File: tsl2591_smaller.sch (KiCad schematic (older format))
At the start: 7 parts, among them J1 Conn_01x04_Female, Q1 BSS138, Q2 BSS138, U1 TSL2591

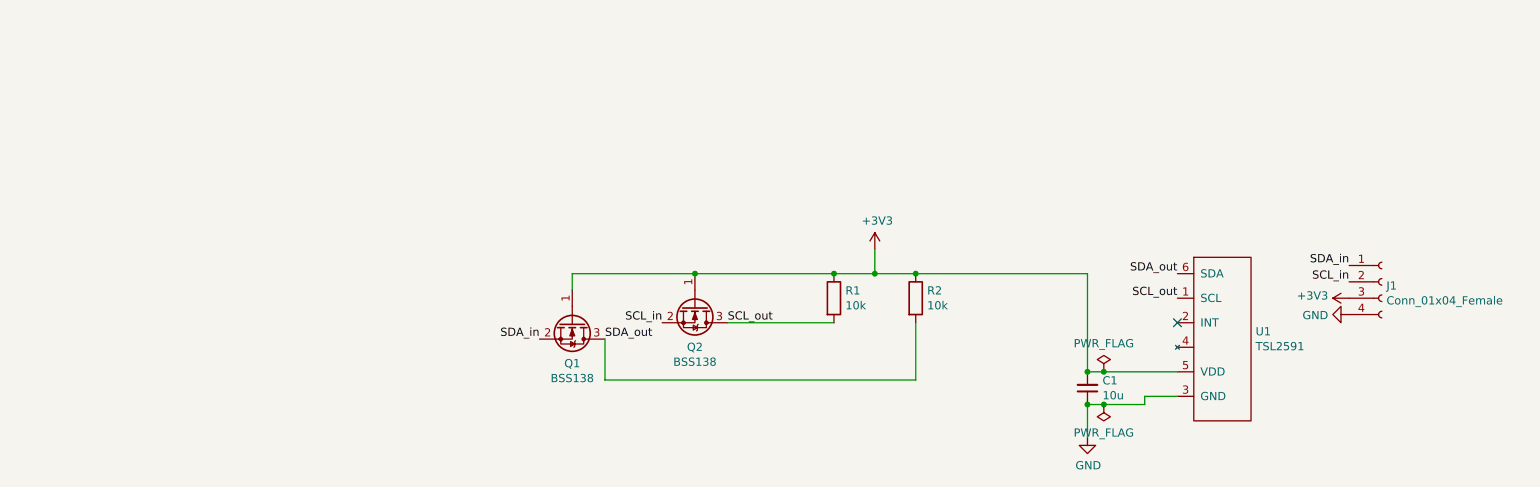
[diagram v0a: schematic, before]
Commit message: Removed more components
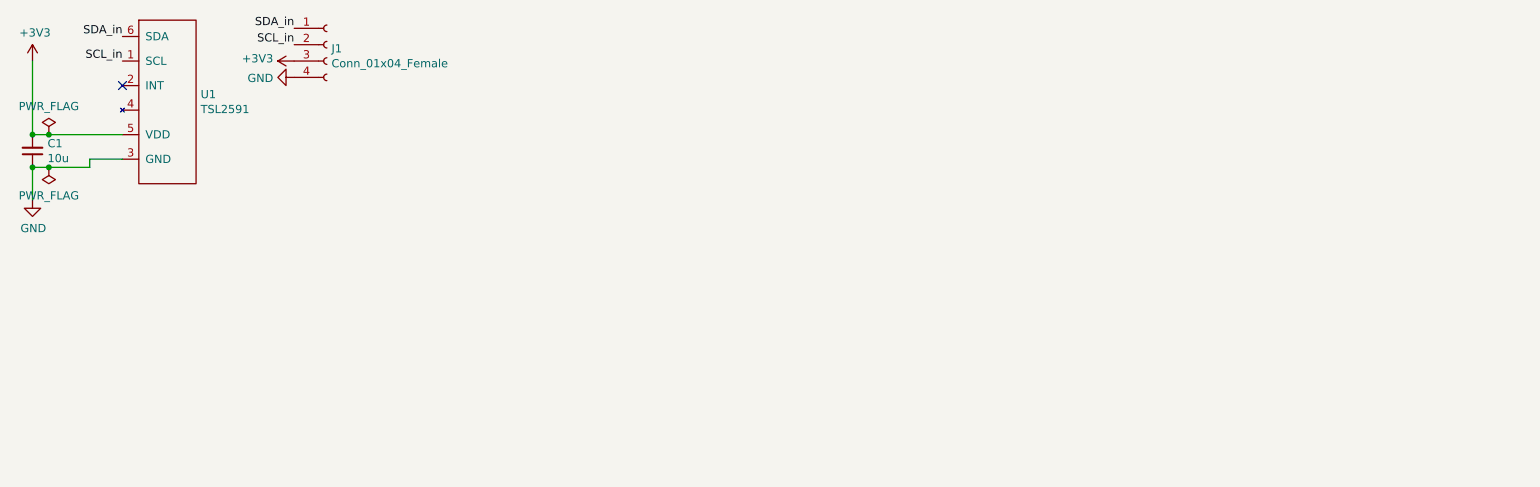
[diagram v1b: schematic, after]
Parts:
- removed Q1, Q2: BSS138, TO_SOT_Packages_SMD:SOT-23, symbol Transistor_FET:BSS138
- removed R1, R2: 10k, Resistors_SMD:R_0805, symbol Device:R
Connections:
- net SCL_out is gone; now on net SCL_in: U1.1 (SCL)
- net SDA_out is gone; now on net SDA_in: U1.6 (SDA)
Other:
- moved on the sheet: C1, J1, U1
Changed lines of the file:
@@
 encoding utf-8
 Sheet 1 1
-Title ""
-Date ""
-Rev ""
-Comp ""
-Comment1 ""
-Comment2 ""
+Title "TSL2591 Board"
+Date "2021-03-06"
+Rev "1.0.0"
+Comp "UTSVT"
+Comment1 "Matthew Yu"
+Comment2 "Jacob Pustilnik"
 Comment3 ""
 Comment4 ""
 $EndDescr
 $Comp
-L Transistor_FET:BSS138 Q1
-U 1 1 6004C224
-P 4350 2650
-F 0 "Q1" V 4599 2650 50  0000 C CNN
-F 1 "BSS138" V 4690 2650 50  0000 C CNN
-F 2 "TO_SOT_Packages_SMD:SOT-23" H 4550 2575 50  0001 L CIN
-F 3 "https://www.fairchildsemi.com/datasheets/BS/BSS138.pdf" H 4350 2650 50  0001 L CNN
-	1    4350 2650
-	0    1    1    0
-$EndComp
-$Comp
-L Transistor_FET:BSS138 Q2
-U 1 1 6004F25D
-P 5100 2550
-F 0 "Q2" V 5349 2550 50  0000 C CNN
-F 1 "BSS138" V 5440 2550 50  0000 C CNN
-F 2 "TO_SOT_Packages_SMD:SOT-23" H 5300 2475 50  0001 L CIN
-F 3 "https://www.fairchildsemi.com/datasheets/BS/BSS138.pdf" H 5100 2550 50  0001 L CNN
-	1    5100 2550
-	0    1    1    0
-$EndComp
-$Comp
-L Device:R R1
-U 1 1 6005217F
-P 5950 2500
-F 0 "R1" H 6020 2546 50  0000 L CNN
-F 1 "10k" H 6020 2455 50  0000 L CNN
-F 2 "Resistors_SMD:R_0805" V 5880 2500 50  0001 C CNN
-F 3 "~" H 5950 2500 50  0001 C CNN
-	1    5950 2500
+L power:+3V3 #PWR01
+U 1 1 60054825
+P 1050 1050
+F 0 "#PWR01" H 1050 900 50  0001 C CNN
+F 1 "+3V3" H 1065 1223 50  0000 C CNN
+F 2 "" H 1050 1050 50  0001 C CNN
+F 3 "" H 1050 1050 50  0001 C CNN
+	1    1050 1050
 	1    0    0    -1
 $EndComp
 $Comp
-L power:+3V3 #PWR01
-U 1 1 60054825
-P 6200 2200
-F 0 "#PWR01" H 6200 2050 50  0001 C CNN
-F 1 "+3V3" H 6215 2373 50  0000 C CNN
-F 2 "" H 6200 2200 50  0001 C CNN
-F 3 "" H 6200 2200 50  0001 C CNN
-	1    6200 2200
-	1    0    0    -1
+L tsl2591_smaller:TSL2591 U1
+U 1 1 60064A60
+P 2200 1300
+F 0 "U1" V 2154 1178 50  0000 L CNN
+F 1 "TSL2591" V 2245 1178 50  0000 L CNN
+F 2 "tsl2591_smaller:tsl2591" H 2200 1300 50  0001 C CNN
+F 3 "" H 2200 1300 50  0001 C CNN
+	1    2200 1300
+	0    1    1    0
 $EndComp
+Wire Wire Line
+	1050 1500 1150 1500
 $Comp
-L Device:R R2
-U 1 1 60053D35
-P 6450 2500
-F 0 "R2" H 6520 2546 50  0000 L CNN
-F 1 "10k" H 6520 2455 50  0000 L CNN
-F 2 "Resistors_SMD:R_0805" V 6380 2500 50  0001 C CNN
-F 3 "~" H 6450 2500 50  0001 C CNN
-	1    6450 2500
+L Device:C_Small C1
+U 1 1 6006B095
+P 1050 1600
+F 0 "C1" H 958 1554 50  0000 R CNN
+F 1 "10u" H 958 1645 50  0000 R CNN
+F 2 "Resistors_SMD:R_0805" H 1050 1600 50  0001 C CNN
+F 3 "~" H 1050 1600 50  0001 C CNN
+	1    1050 1600
+	-1   0    0    1
+$EndComp
+Wire Wire Line
+	1050 1700 1150 1700
+Wire Wire Line
+	1400 1700 1400 1650
+$Comp
+L power:GND #PWR02
+U 1 1 6006E387
+P 1050 1900
+F 0 "#PWR02" H 1050 1650 50  0001 C CNN
+F 1 "GND" H 1055 1727 50  0000 C CNN
+F 2 "" H 1050 1900 50  0001 C CNN
+F 3 "" H 1050 1900 50  0001 C CNN
+	1    1050 1900
 	1    0    0    -1
 $EndComp
 Wire Wire Line
-	5950 2350 6200 2350
-Wire Wire Line
-	6200 2200 6200 2350
-Connection ~ 6200 2350
-Wire Wire Line
-	6200 2350 6450 2350
-Wire Wire Line
-	5950 2350 5100 2350
-Connection ~ 5950 2350
-Wire Wire Line
-	5100 2350 4350 2350
-Wire Wire Line
-	4350 2350 4350 2450
-Connection ~ 5100 2350
-Text Label 4150 2750 2    50   ~ 0
+	1050 1900 1050 1700
+Connection ~ 1050 1700
+Text Label 1600 1050 2    50   ~ 0
+SCL_in
+NoConn ~ 1600 1200
+Text Label 1600 900  2    50   ~ 0
 SDA_in
-Text Label 4550 2750 0    50   ~ 0
-SDA_out
-Text Label 4900 2650 2    50   ~ 0
-SCL_in
-Text Label 5300 2650 0    50   ~ 0
-SCL_out
-Wire Wire Line
-	5950 2650 5300 2650
-Wire Wire Line
-	6450 2650 6450 3000
-Wire Wire Line
-	6450 3000 4550 3000
-Wire Wire Line
-	4550 3000 4550 2750
-$Comp
-L tsl2591_smaller:TSL2591 U1
-U 1 1 60064A60
-P 8650 2750
-F 0 "U1" V 8604 2628 50  0000 L CNN
-F 1 "TSL2591" V 8695 2628 50  0000 L CNN
-F 2 "tsl2591_smaller:tsl2591" H 8650 2750 50  0001 C CNN
-F 3 "" H 8650 2750 50  0001 C CNN
-	1    8650 2750
-	0    1    1    0
-$EndComp
-Wire Wire Line
-	6450 2350 7500 2350
-Wire Wire Line
-	7500 2350 7500 2950
-Wire Wire Line
-	7500 2950 7600 2950
-Connection ~ 6450 2350
-$Comp
-L Device:C_Small C1
-U 1 1 6006B095
-P 7500 3050
-F 0 "C1" H 7408 3004 50  0000 R CNN
-F 1 "10u" H 7408 3095 50  0000 R CNN
-F 2 "Resistors_SMD:R_0805" H 7500 3050 50  0001 C CNN
-F 3 "~" H 7500 3050 50  0001 C CNN
-	1    7500 3050
-	-1   0    0    1
-$EndComp
-Connection ~ 7500 2950
-Wire Wire Line
-	7500 3150 7600 3150
-Wire Wire Line
-	7850 3150 7850 3100
-$Comp
-L power:GND #PWR02
-U 1 1 6006E387
-P 7500 3350
-F 0 "#PWR02" H 7500 3100 50  0001 C CNN
-F 1 "GND" H 7505 3177 50  0000 C CNN
-F 2 "" H 7500 3350 50  0001 C CNN
-F 3 "" H 7500 3350 50  0001 C CNN
-	1    7500 3350
-	1    0    0    -1
-$EndComp
-Wire Wire Line
-	7500 3350 7500 3150
-Connection ~ 7500 3150
-Text Label 8050 2500 2    50   ~ 0
-SCL_out
-NoConn ~ 8050 2650
-Text Label 8050 2350 2    50   ~ 0
-SDA_out
 $Comp
 L power:+3V3 #PWR03
 U 1 1 6007AD26
-P 9100 2500
-F 0 "#PWR03" H 9100 2350 50  0001 C CNN
-F 1 "+3V3" V 9115 2628 50  0000 L CNN
-F 2 "" H 9100 2500 50  0001 C CNN
-F 3 "" H 9100 2500 50  0001 C CNN
-	1    9100 2500
+P 2650 1050
+F 0 "#PWR03" H 2650 900 50  0001 C CNN
+F 1 "+3V3" V 2665 1178 50  0000 L CNN
+F 2 "" H 2650 1050 50  0001 C CNN
+F 3 "" H 2650 1050 50  0001 C CNN
+	1    2650 1050
 	0    -1   -1   0
 $EndComp
@@
 L power:GND #PWR04
 U 1 1 6007BFAB
-P 9100 2600
-F 0 "#PWR04" H 9100 2350 50  0001 C CNN
-F 1 "GND" V 9105 2472 50  0000 R CNN
-F 2 "" H 9100 2600 50  0001 C CNN
-F 3 "" H 9100 2600 50  0001 C CNN
-	1    9100 2600
+P 2650 1150
+F 0 "#PWR04" H 2650 900 50  0001 C CNN
+F 1 "GND" V 2655 1022 50  0000 R CNN
+F 2 "" H 2650 1150 50  0001 C CNN
+F 3 "" H 2650 1150 50  0001 C CNN
+	1    2650 1150
 	0    1    1    0
 $EndComp
@@
 L Connector:Conn_01x04_Female J1
 U 1 1 60074FEE
-P 9300 2400
-F 0 "J1" H 9328 2376 50  0000 L CNN
-F 1 "Conn_01x04_Female" H 9328 2285 50  0000 L CNN
-F 2 "Connector_PinHeader_2.54mm:PinHeader_2x02_P2.54mm_Vertical_SMD" H 9300 2400 50  0001 C CNN
-F 3 "~" H 9300 2400 50  0001 C CNN
-	1    9300 2400
+P 2850 950
+F 0 "J1" H 2878 926 50  0000 L CNN
+F 1 "Conn_01x04_Female" H 2878 835 50  0000 L CNN
+F 2 "Connector_PinHeader_2.54mm:PinHeader_2x02_P2.54mm_Vertical_SMD" H 2850 950 50  0001 C CNN
+F 3 "~" H 2850 950 50  0001 C CNN
+	1    2850 950
 	1    0    0    -1
 $EndComp
-Text Label 9100 2300 2    50   ~ 0
+Text Label 2650 850  2    50   ~ 0
 SDA_in
-Text Label 9100 2400 2    50   ~ 0
+Text Label 2650 950  2    50   ~ 0
 SCL_in
 $Comp
 L MPPT-rescue:PWR_FLAG #FLG01
 U 1 1 6007E378
-P 7600 2950
-F 0 "#FLG01" H 7600 3025 50  0001 C CNN
-F 1 "PWR_FLAG" H 7600 3123 50  0000 C CNN
-F 2 "" H 7600 2950 50  0001 C CNN
-F 3 "" H 7600 2950 50  0001 C CNN
-	1    7600 2950
+P 1150 1500
+F 0 "#FLG01" H 1150 1575 50  0001 C CNN
+F 1 "PWR_FLAG" H 1150 1673 50  0000 C CNN
+F 2 "" H 1150 1500 50  0001 C CNN
+F 3 "" H 1150 1500 50  0001 C CNN
+	1    1150 1500
 	1    0    0    -1
 $EndComp
@@
 L MPPT-rescue:PWR_FLAG #FLG02
 U 1 1 60080A8B
-P 7600 3150
-F 0 "#FLG02" H 7600 3225 50  0001 C CNN
-F 1 "PWR_FLAG" H 7600 3323 50  0000 C CNN
-F 2 "" H 7600 3150 50  0001 C CNN
-F 3 "" H 7600 3150 50  0001 C CNN
-	1    7600 3150
+P 1150 1700
+F 0 "#FLG02" H 1150 1775 50  0001 C CNN
+F 1 "PWR_FLAG" H 1150 1873 50  0000 C CNN
+F 2 "" H 1150 1700 50  0001 C CNN
+F 3 "" H 1150 1700 50  0001 C CNN
+	1    1150 1700
 	-1   0    0    1
 $EndComp
-Connection ~ 7600 2950
-Connection ~ 7600 3150
+Connection ~ 1150 1500
+Connection ~ 1150 1700
 Wire Wire Line
-	7600 3150 7850 3150
+	1150 1700 1400 1700
 Wire Wire Line
-	7850 3100 8050 3100
+	1400 1650 1600 1650
 Wire Wire Line
-	7600 2950 8050 2950
+	1150 1500 1600 1500
+Wire Wire Line
+	1050 1500 1050 1050
+Connection ~ 1050 1500
 $EndSCHEMATC
